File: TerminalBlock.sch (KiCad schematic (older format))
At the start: 0 parts

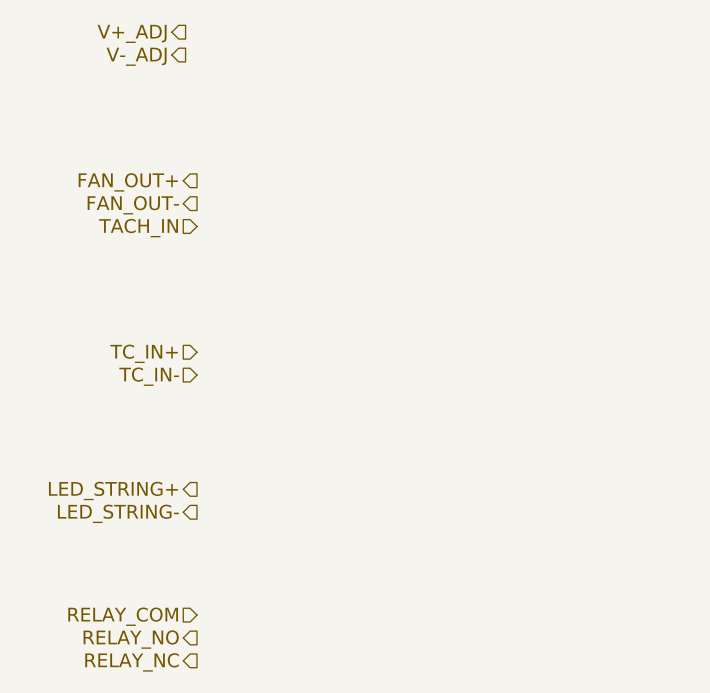
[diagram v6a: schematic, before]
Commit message: 5.6 Video 1/2 Associating and Placing the Terminal/ATX Blocks
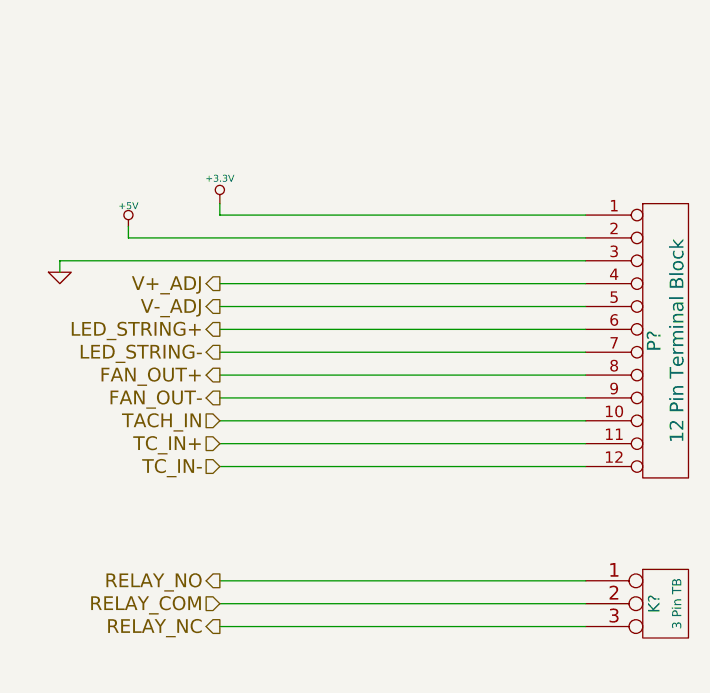
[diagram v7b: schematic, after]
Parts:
- added K?: 3 Pin TB, symbol CONN_3
- added P?: 12 Pin Terminal Block, symbol CONN_12
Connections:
- net FAN_OUT+: now also P?.8 (P8)
- net FAN_OUT-: now also P?.9 (P9)
- net LED_STRING+: now also P?.6 (P6)
- net LED_STRING-: now also P?.7 (P7)
- net RELAY_COM: now also K?.2 (PM)
- net RELAY_NC: now also K?.3 (P3)
- net RELAY_NO: now also K?.1 (P1)
- net TACH_IN: now also P?.10 (P10)
- net TC_IN+: now also P?.11 (P11)
- net TC_IN-: now also P?.12 (P12)
- net V+_ADJ: now also P?.4 (P4)
- net V-_ADJ: now also P?.5 (P5)
- new net +3.3V: P?.1 (P1)
- new net +5V: P?.2 (P2)
- new net GND: P?.3 (P3)
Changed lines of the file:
@@
 LIBS:BenchBudEE
 LIBS:BenchBudEE-cache
-EELAYER 24 0
+EELAYER 27 0
 EELAYER END
 $Descr A4 11693 8268
 encoding utf-8
-Sheet 6 9
+Sheet 5 9
 Title ""
-Date "21 feb 2014"
+Date "22 feb 2014"
 Rev ""
 Comp ""
@@
 Comment4 ""
 $EndDescr
-Text HLabel 1550 1000 0    60   Output ~ 0
+Text HLabel 1700 2100 0    60   Output ~ 0
 V+_ADJ
-Text HLabel 1550 1100 0    60   Output ~ 0
+Text HLabel 1700 2200 0    60   Output ~ 0
 V-_ADJ
-Text HLabel 1600 1650 0    60   Output ~ 0
+Text HLabel 1700 2500 0    60   Output ~ 0
 FAN_OUT+
-Text HLabel 1600 1750 0    60   Output ~ 0
+Text HLabel 1700 2600 0    60   Output ~ 0
 FAN_OUT-
-Text HLabel 1600 1850 0    60   Input ~ 0
+Text HLabel 1700 2700 0    60   Input ~ 0
 TACH_IN
-Text HLabel 1600 2400 0    60   Input ~ 0
+Text HLabel 1700 2800 0    60   Input ~ 0
 TC_IN+
-Text HLabel 1600 2500 0    60   Input ~ 0
+Text HLabel 1700 2900 0    60   Input ~ 0
 TC_IN-
-Text HLabel 1600 3000 0    60   Output ~ 0
+Text HLabel 1700 2300 0    60   Output ~ 0
 LED_STRING+
-Text HLabel 1600 3100 0    60   Output ~ 0
+Text HLabel 1700 2400 0    60   Output ~ 0
 LED_STRING-
-Text HLabel 1600 3550 0    60   Input ~ 0
+Text HLabel 1700 3500 0    60   Input ~ 0
 RELAY_COM
-Text HLabel 1600 3650 0    60   Output ~ 0
+Text HLabel 1700 3400 0    60   Output ~ 0
 RELAY_NO
-Text HLabel 1600 3750 0    60   Output ~ 0
+Text HLabel 1700 3600 0    60   Output ~ 0
 RELAY_NC
+$Comp
+L +3.3V #PWR?
+U 1 1 53083814
+P 1700 1750
+F 0 "#PWR?" H 1700 1710 30  0001 C CNN
+F 1 "+3.3V" H 1700 1860 30  0000 C CNN
+F 2 "" H 1700 1750 60  0000 C CNN
+F 3 "" H 1700 1750 60  0000 C CNN
+	1    1700 1750
+	1    0    0    -1
+$EndComp
+$Comp
+L CONN_12 P?
+U 1 1 53083823
+P 3650 2350
+F 0 "P?" V 3600 2350 60  0000 C CNN
+F 1 "12 Pin Terminal Block" V 3700 2350 60  0000 C CNN
+F 2 "" H 3650 2350 60  0000 C CNN
+F 3 "http://media.digikey.com/pdf/Data%20Sheets/Phoenix%20Contact%20PDFs/1706251.pdf" H 3650 2350 60  0001 C CNN
+F 4 "Phoenix Contact" H 3650 2350 60  0001 C CNN "MFG Name"
+F 5 "1706251" H 3650 2350 60  0001 C CNN "MFG Part Number"
+	1    3650 2350
+	1    0    0    -1
+$EndComp
+$Comp
+L +5V #PWR?
+U 1 1 5308384C
+P 1300 1850
+F 0 "#PWR?" H 1300 1940 20  0001 C CNN
+F 1 "+5V" H 1300 1940 30  0000 C CNN
+F 2 "" H 1300 1850 60  0000 C CNN
+F 3 "" H 1300 1850 60  0000 C CNN
+	1    1300 1850
+	1    0    0    -1
+$EndComp
+$Comp
+L GND #PWR?
+U 1 1 5308385B
+P 1000 2050
+F 0 "#PWR?" H 1000 2050 30  0001 C CNN
+F 1 "GND" H 1000 1980 30  0001 C CNN
+F 2 "" H 1000 2050 60  0000 C CNN
+F 3 "" H 1000 2050 60  0000 C CNN
+	1    1000 2050
+	1    0    0    -1
+$EndComp
+Wire Wire Line
+	1700 1800 3300 1800
+Wire Wire Line
+	1300 1900 3300 1900
+Wire Wire Line
+	3300 2000 1000 2000
+Wire Wire Line
+	1000 2000 1000 2050
+Wire Wire Line
+	1700 2100 3300 2100
+Wire Wire Line
+	3300 2200 1700 2200
+Wire Wire Line
+	1700 2300 3300 2300
+Wire Wire Line
+	3300 2400 1700 2400
+Wire Wire Line
+	1700 2500 3300 2500
+Wire Wire Line
+	3300 2600 1700 2600
+Wire Wire Line
+	1700 2700 3300 2700
+Wire Wire Line
+	3300 2800 1700 2800
+Wire Wire Line
+	1700 2900 3300 2900
+Wire Wire Line
+	1700 1750 1700 1800
+Wire Wire Line
+	1300 1850 1300 1900
+$Comp
+L CONN_3 K?
+U 1 1 5308394B
+P 3650 3500
+F 0 "K?" V 3600 3500 50  0000 C CNN
+F 1 "3 Pin TB" V 3700 3500 40  0000 C CNN
+F 2 "" H 3650 3500 60  0000 C CNN
+F 3 "http://media.digikey.com/pdf/Data%20Sheets/Phoenix%20Contact%20PDFs/1990986.pdf" H 3650 3500 60  0001 C CNN
+F 4 "Phoenix Contact" H 3650 3500 60  0001 C CNN "MFG Name"
+F 5 "1990986" H 3650 3500 60  0001 C CNN "MFG Part Number"
+	1    3650 3500
+	1    0    0    -1
+$EndComp
+Wire Wire Line
+	3300 3400 1700 3400
+Wire Wire Line
+	3300 3500 1700 3500
+Wire Wire Line
+	3300 3600 1700 3600
 $EndSCHEMATC

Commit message: 5.6 Video 2/2 Associating and Placing the Terminal/ATX Blocks
Created the 12pin, 3 pin and atx connector footprints and placed
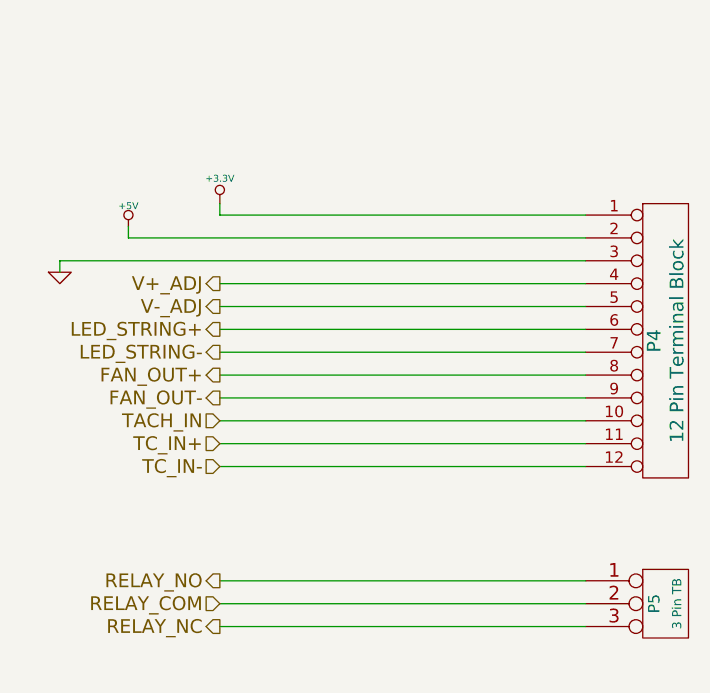
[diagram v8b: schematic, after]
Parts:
- gave numbers to parts that had none: 2
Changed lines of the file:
@@
 RELAY_NC
 $Comp
-L +3.3V #PWR?
+L +3.3V #PWR22
 U 1 1 53083814
 P 1700 1750
-F 0 "#PWR?" H 1700 1710 30  0001 C CNN
+F 0 "#PWR22" H 1700 1710 30  0001 C CNN
 F 1 "+3.3V" H 1700 1860 30  0000 C CNN
 F 2 "" H 1700 1750 60  0000 C CNN
@@
 $EndComp
 $Comp
-L CONN_12 P?
+L CONN_12 P4
 U 1 1 53083823
 P 3650 2350
-F 0 "P?" V 3600 2350 60  0000 C CNN
+F 0 "P4" V 3600 2350 60  0000 C CNN
 F 1 "12 Pin Terminal Block" V 3700 2350 60  0000 C CNN
 F 2 "" H 3650 2350 60  0000 C CNN
@@
 $EndComp
 $Comp
-L +5V #PWR?
+L +5V #PWR21
 U 1 1 5308384C
 P 1300 1850
-F 0 "#PWR?" H 1300 1940 20  0001 C CNN
+F 0 "#PWR21" H 1300 1940 20  0001 C CNN
 F 1 "+5V" H 1300 1940 30  0000 C CNN
 F 2 "" H 1300 1850 60  0000 C CNN
@@
 $EndComp
 $Comp
-L GND #PWR?
+L GND #PWR20
 U 1 1 5308385B
 P 1000 2050
-F 0 "#PWR?" H 1000 2050 30  0001 C CNN
+F 0 "#PWR20" H 1000 2050 30  0001 C CNN
 F 1 "GND" H 1000 1980 30  0001 C CNN
 F 2 "" H 1000 2050 60  0000 C CNN
@@
 	1300 1850 1300 1900
 $Comp
-L CONN_3 K?
+L CONN_3 P5
 U 1 1 5308394B
 P 3650 3500
-F 0 "K?" V 3600 3500 50  0000 C CNN
+F 0 "P5" V 3600 3500 50  0000 C CNN
 F 1 "3 Pin TB" V 3700 3500 40  0000 C CNN
 F 2 "" H 3650 3500 60  0000 C CNN
